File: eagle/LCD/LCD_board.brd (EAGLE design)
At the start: 100.5 x 81.4 mm, 7 parts, among them CN1 1X4-CLEANBIG

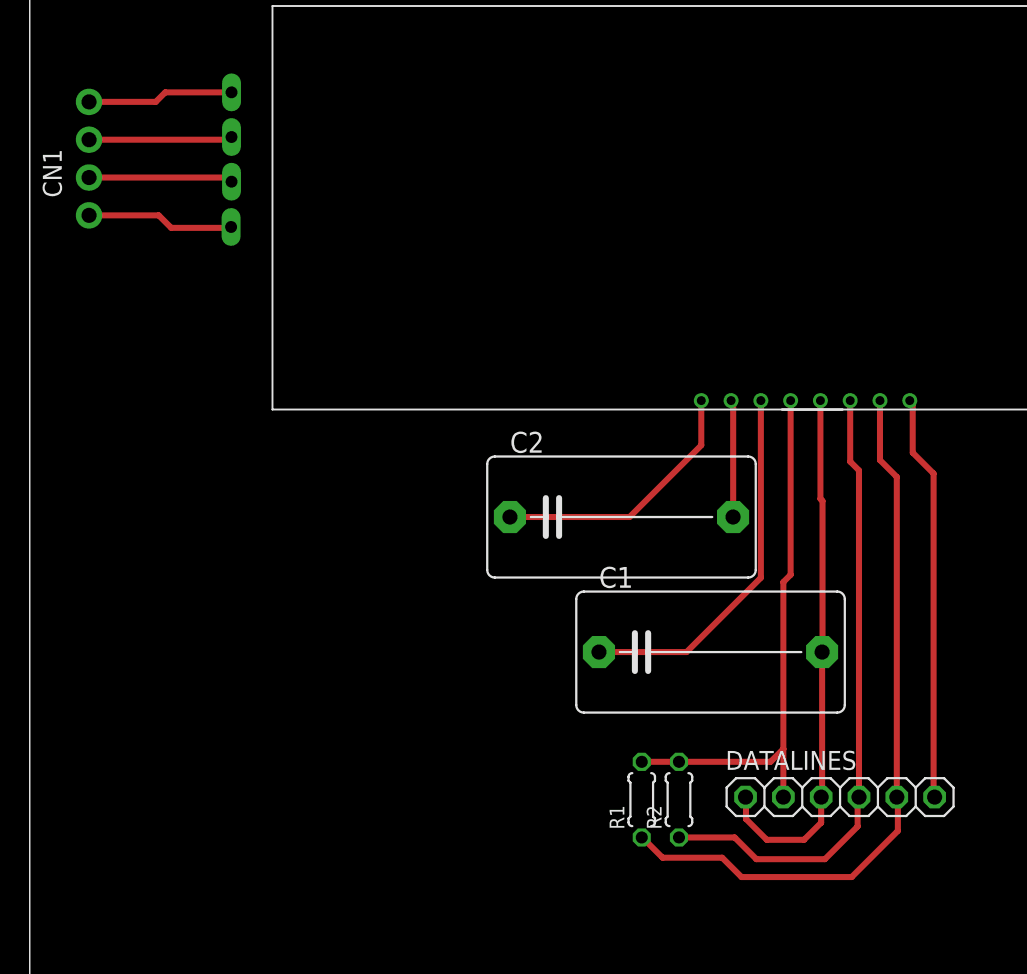
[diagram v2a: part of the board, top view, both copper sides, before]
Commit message: Routed LCD From Bottom
Routed from bottom. Have it closer to what we need to ask Andrew for
suggestions on LED Hole (currently is not wide enough)
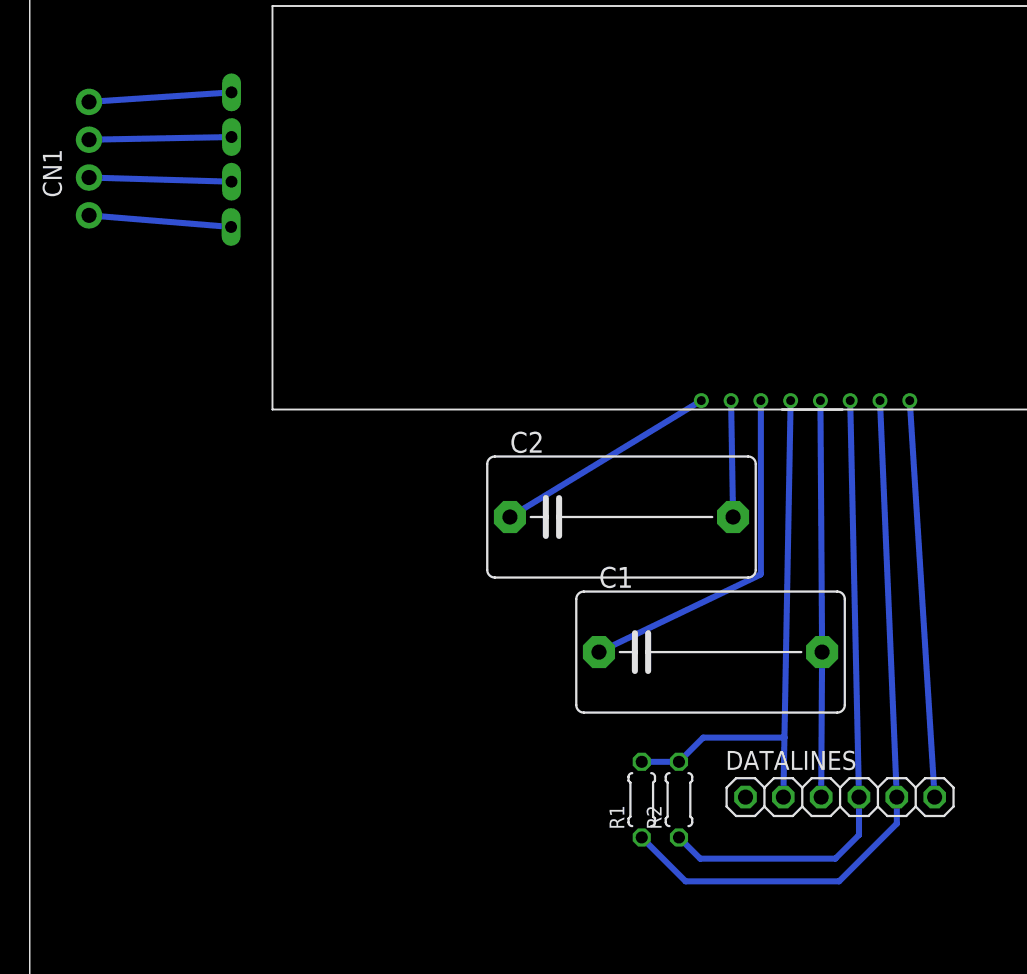
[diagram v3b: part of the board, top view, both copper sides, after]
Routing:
- net GND: track 36.0 -> 26.6 mm
- net N$1: track 17.8 -> 15.0 mm
- net N$5: track 24.8 -> 23.7 mm
- net RST: track 27.3 -> 26.7 mm
- net SCL: track 49.0 -> 48.4 mm
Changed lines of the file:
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@@
 <?xml version="1.0" encoding="utf-8"?>
 <!DOCTYPE eagle SYSTEM "eagle.dtd">
-<eagle version="6.6.0">
+<eagle version="7.0.0">
 <drawing>
 <settings>
@@
 <setting verticaltext="up"/>
 </settings>
-<grid distance="0.1" unitdist="mm" unit="mm" style="lines" multiple="1" display="yes" altdistance="0.025" altunitdist="inch" altunit="inch"/>
+<grid distance="0.01" unitdist="inch" unit="inch" style="lines" multiple="1" display="yes" altdistance="0.025" altunitdist="inch" altunit="inch"/>
 <layers>
 <layer number="1" name="Top" color="4" fill="1" visible="yes" active="yes"/>
@@
 <pass name="Default">
 <param name="RoutingGrid" value="50mil"/>
+<param name="AutoGrid" value="1"/>
+<param name="Efforts" value="0"/>
+<param name="TopRouterVariant" value="1"/>
 <param name="tpViaShape" value="round"/>
 <param name="PrefDir.1" value="|"/>
@@
 <contactref element="C2" pad="1"/>
 <contactref element="U$1" pad="P$8"/>
-<wire x1="32.247" y1="31.58" x2="40.28" y2="31.58" width="0.4064" layer="1"/>
-<wire x1="40.28" y1="31.58" x2="45.1" y2="36.4" width="0.4064" layer="1"/>
-<wire x1="45.1" y1="36.4" x2="45.1" y2="39.4" width="0.4064" layer="1"/>
+<wire x1="45.1" y1="39.4" x2="32.247" y2="31.58" width="0.4064" layer="16"/>
 </signal>
 <signal name="C1+">
 <contactref element="C2" pad="2"/>
 <contactref element="U$1" pad="P$7"/>
-<wire x1="47.24" y1="31.587" x2="47.24" y2="39.26" width="0.4064" layer="1"/>
-<wire x1="47.24" y1="39.26" x2="47.1" y2="39.4" width="0.4064" layer="1"/>
-<wire x1="47.24" y1="31.587" x2="47.233" y2="31.58" width="0" layer="19" extent="1-1"/>
+<wire x1="47.1" y1="39.4" x2="47.233" y2="31.58" width="0.4064" layer="16"/>
 </signal>
 <signal name="RST">
 <contactref element="DATALINES" pad="6"/>
-<wire x1="60.7" y1="12.84" x2="60.77" y2="12.77" width="0.4064" layer="1"/>
 <contactref element="U$1" pad="P$1"/>
-<wire x1="60.7" y1="12.84" x2="60.7" y2="34.5" width="0.4064" layer="1"/>
-<wire x1="60.7" y1="34.5" x2="59.3" y2="35.9" width="0.4064" layer="1"/>
-<wire x1="59.3" y1="35.9" x2="59.3" y2="39.2" width="0.4064" layer="1"/>
-<wire x1="59.3" y1="39.2" x2="59.1" y2="39.4" width="0.4064" layer="1"/>
+<wire x1="59.1" y1="39.4" x2="60.77" y2="12.77" width="0.4064" layer="16"/>
 </signal>
 <signal name="SCL">
@@
 <contactref element="R1" pad="1"/>
 <contactref element="U$1" pad="P$2"/>
-<wire x1="58.23" y1="12.77" x2="58.23" y2="34.27" width="0.4064" layer="1"/>
-<wire x1="58.23" y1="34.27" x2="57.1" y2="35.4" width="0.4064" layer="1"/>
-<wire x1="57.1" y1="35.4" x2="57.1" y2="39.4" width="0.4064" layer="1"/>
-<wire x1="41.1" y1="10.06" x2="41.14" y2="10.06" width="0.4064" layer="1"/>
-<wire x1="41.14" y1="10.06" x2="42.5" y2="8.7" width="0.4064" layer="1"/>
-<wire x1="42.5" y1="8.7" x2="46.5" y2="8.7" width="0.4064" layer="1"/>
-<wire x1="46.5" y1="8.7" x2="47.8" y2="7.4" width="0.4064" layer="1"/>
-<wire x1="47.8" y1="7.4" x2="55.2" y2="7.4" width="0.4064" layer="1"/>
-<wire x1="55.2" y1="7.4" x2="58.3" y2="10.5" width="0.4064" layer="1"/>
-<wire x1="58.3" y1="10.5" x2="58.3" y2="12.7" width="0.4064" layer="1"/>
-<wire x1="58.3" y1="12.7" x2="58.23" y2="12.77" width="0.4064" layer="1"/>
+<wire x1="57.1" y1="39.4" x2="58.23" y2="12.77" width="0.4064" layer="16"/>
+<wire x1="41.1" y1="10.06" x2="44.048" y2="7.112" width="0.4064" layer="16"/>
+<wire x1="44.048" y1="7.112" x2="54.356" y2="7.112" width="0.4064" layer="16"/>
+<wire x1="54.356" y1="7.112" x2="58.23" y2="10.986" width="0.4064" layer="16"/>
+<wire x1="58.23" y1="10.986" x2="58.23" y2="12.77" width="0.4064" layer="16"/>
 </signal>
 <signal name="SDA">
@@
 <contactref element="R2" pad="1"/>
 <contactref element="U$1" pad="P$3"/>
-<wire x1="55.69" y1="12.77" x2="55.69" y2="34.71" width="0.4064" layer="1"/>
-<wire x1="55.69" y1="34.71" x2="55.1" y2="35.3" width="0.4064" layer="1"/>
-<wire x1="55.1" y1="35.3" x2="55.1" y2="39.4" width="0.4064" layer="1"/>
-<wire x1="43.6" y1="10.06" x2="47.34" y2="10.06" width="0.4064" layer="1"/>
-<wire x1="47.34" y1="10.06" x2="48.8" y2="8.6" width="0.4064" layer="1"/>
-<wire x1="48.8" y1="8.6" x2="53.4" y2="8.6" width="0.4064" layer="1"/>
-<wire x1="53.4" y1="8.6" x2="55.6" y2="10.8" width="0.4064" layer="1"/>
-<wire x1="55.6" y1="10.8" x2="55.6" y2="12.68" width="0.4064" layer="1"/>
-<wire x1="55.6" y1="12.68" x2="55.69" y2="12.77" width="0.4064" layer="1"/>
+<wire x1="55.1" y1="39.4" x2="55.69" y2="12.77" width="0.4064" layer="16"/>
+<wire x1="43.6" y1="10.06" x2="45.024" y2="8.636" width="0.4064" layer="16"/>
+<wire x1="45.024" y1="8.636" x2="54.102" y2="8.636" width="0.4064" layer="16"/>
+<wire x1="54.102" y1="8.636" x2="55.69" y2="10.224" width="0.4064" layer="16"/>
+<wire x1="55.69" y1="10.224" x2="55.69" y2="12.77" width="0.4064" layer="16"/>
 </signal>
 <signal name="VDD">
@@
 <contactref element="R2" pad="2"/>
 <contactref element="U$1" pad="P$5"/>
-<wire x1="50.61" y1="12.77" x2="50.61" y2="16" width="0.4064" layer="1"/>
-<wire x1="50.61" y1="16" x2="50.61" y2="27.21" width="0.4064" layer="1"/>
-<wire x1="50.61" y1="27.21" x2="51.1" y2="27.7" width="0.4064" layer="1"/>
-<wire x1="51.1" y1="27.7" x2="51.1" y2="39.4" width="0.4064" layer="1"/>
-<wire x1="41.1" y1="15.14" x2="43.6" y2="15.14" width="0.4064" layer="1"/>
-<wire x1="43.6" y1="15.14" x2="49.75" y2="15.14" width="0.4064" layer="1"/>
-<wire x1="49.75" y1="15.14" x2="50.61" y2="16" width="0.4064" layer="1"/>
+<wire x1="51.1" y1="39.4" x2="50.68353125" y2="16.76614375" width="0.4064" layer="16"/>
+<wire x1="50.68353125" y1="16.76614375" x2="50.61" y2="12.77" width="0.4064" layer="16"/>
+<wire x1="41.1" y1="15.14" x2="43.6" y2="15.14" width="0.4064" layer="16"/>
+<wire x1="43.6" y1="15.14" x2="45.22614375" y2="16.76614375" width="0.4064" layer="16"/>
+<wire x1="45.22614375" y1="16.76614375" x2="50.68353125" y2="16.76614375" width="0.4064" layer="16"/>
 </signal>
 <signal name="GND">
@@
 <contactref element="DATALINES" pad="3"/>
 <contactref element="C1" pad="2"/>
-<wire x1="53.24" y1="22.537" x2="53.213" y2="22.51" width="0.4064" layer="1"/>
-<wire x1="53.213" y1="22.51" x2="53.213" y2="12.833" width="0.4064" layer="1"/>
-<wire x1="53.213" y1="12.833" x2="53.15" y2="12.77" width="0.4064" layer="1"/>
-<wire x1="53.15" y1="12.77" x2="53.15" y2="11.05" width="0.4064" layer="1"/>
-<wire x1="53.15" y1="11.05" x2="52" y2="9.9" width="0.4064" layer="1"/>
-<wire x1="52" y1="9.9" x2="49.5" y2="9.9" width="0.4064" layer="1"/>
-<wire x1="49.5" y1="9.9" x2="48.1" y2="11.3" width="0.4064" layer="1"/>
-<wire x1="48.1" y1="11.3" x2="48.1" y2="12.74" width="0.4064" layer="1"/>
-<wire x1="48.1" y1="12.74" x2="48.07" y2="12.77" width="0.4064" layer="1"/>
 <contactref element="U$1" pad="P$4"/>
-<wire x1="53.24" y1="22.537" x2="53.24" y2="32.66" width="0.4064" layer="1"/>
-<wire x1="53.24" y1="32.66" x2="53.1" y2="32.8" width="0.4064" layer="1"/>
-<wire x1="53.1" y1="32.8" x2="53.1" y2="39.4" width="0.4064" layer="1"/>
+<wire x1="53.1" y1="39.4" x2="53.213" y2="22.51" width="0.4064" layer="16"/>
+<wire x1="53.213" y1="22.51" x2="53.15" y2="12.77" width="0.4064" layer="16"/>
+<wire x1="48.07" y1="12.77" x2="53.15" y2="12.77" width="0" layer="19" extent="1-1"/>
 </signal>
 <signal name="A">
 <contactref element="CN1" pad="4"/>
 <contactref element="U$1" pad="P$RK"/>
-<wire x1="3.98" y1="59.46" x2="8.46" y2="59.46" width="0.4064" layer="1"/>
-<wire x1="8.46" y1="59.46" x2="9.1" y2="60.1" width="0.4064" layer="1"/>
-<wire x1="9.1" y1="60.1" x2="13.55" y2="60.1" width="0.4064" layer="1"/>
+<wire x1="13.55" y1="60.1" x2="3.98" y2="59.46" width="0.4064" layer="16"/>
 </signal>
 <signal name="GK">
 <contactref element="CN1" pad="2"/>
 <contactref element="U$1" pad="P$BK"/>
-<wire x1="3.98" y1="54.38" x2="13.27" y2="54.38" width="0.4064" layer="1"/>
-<wire x1="13.27" y1="54.38" x2="13.55" y2="54.1" width="0.4064" layer="1"/>
+<wire x1="3.98" y1="54.38" x2="13.55" y2="54.1" width="0.4064" layer="16"/>
 </signal>
 <signal name="N$2">
 <contactref element="CN1" pad="3"/>
 <contactref element="U$1" pad="P$GK"/>
-<wire x1="3.98" y1="56.92" x2="13.37" y2="56.92" width="0.4064" layer="1"/>
-<wire x1="13.37" y1="56.92" x2="13.55" y2="57.1" width="0.4064" layer="1"/>
+<wire x1="13.55" y1="57.1" x2="3.98" y2="56.92" width="0.4064" layer="16"/>
 </signal>
 <signal name="N$4">
 <contactref element="CN1" pad="1"/>
 <contactref element="U$1" pad="P$A"/>
-<wire x1="3.98" y1="51.84" x2="8.66" y2="51.84" width="0.4064" layer="1"/>
-<wire x1="8.66" y1="51.84" x2="9.5" y2="51" width="0.4064" layer="1"/>
-<wire x1="9.5" y1="51" x2="13.46" y2="51" width="0.4064" layer="1"/>
-<wire x1="13.46" y1="51" x2="13.52" y2="51.06" width="0.4064" layer="1"/>
+<wire x1="13.52" y1="51.06" x2="3.98" y2="51.84" width="0.4064" layer="16"/>
 </signal>
 <signal name="N$5">
 <contactref element="U$1" pad="P$6"/>
 <contactref element="C1" pad="1"/>
-<wire x1="38.227" y1="22.51" x2="44.11" y2="22.51" width="0.4064" layer="1"/>
-<wire x1="44.11" y1="22.51" x2="49.1" y2="27.5" width="0.4064" layer="1"/>
-<wire x1="49.1" y1="27.5" x2="49.1" y2="39.4" width="0.4064" layer="1"/>
+<wire x1="49.1" y1="39.4" x2="49.1" y2="27.764" width="0.4064" layer="16"/>
+<wire x1="49.1" y1="27.764" x2="49.022" y2="27.686" width="0.4064" layer="16"/>
+<wire x1="49.022" y1="27.686" x2="38.227" y2="22.51" width="0.4064" layer="16"/>
 </signal>
 </signals>
